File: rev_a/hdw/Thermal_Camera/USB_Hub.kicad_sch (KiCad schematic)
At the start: 1 part

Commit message: duplicated telemetry for all rails, added random tweaks to logic levels of signals
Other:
- note added: "CONSIDER CHANGING TO TUSB2046"
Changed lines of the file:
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@@
     (company "Drew Maatman and Michael Laffin")
+  )
+  (text "CONSIDER CHANGING TO TUSB2046" (at 72.39 38.735 0)
+    (effects (font (face "Courier New") (size 5.08 5.08) (thickness 1.016) bold (color 194 0 0 1)) (justify left bottom))
   )
   (symbol (lib_id "Interface_USB:TUSB2036") (at 131.445 91.44 0) (mirror y) (unit 1)

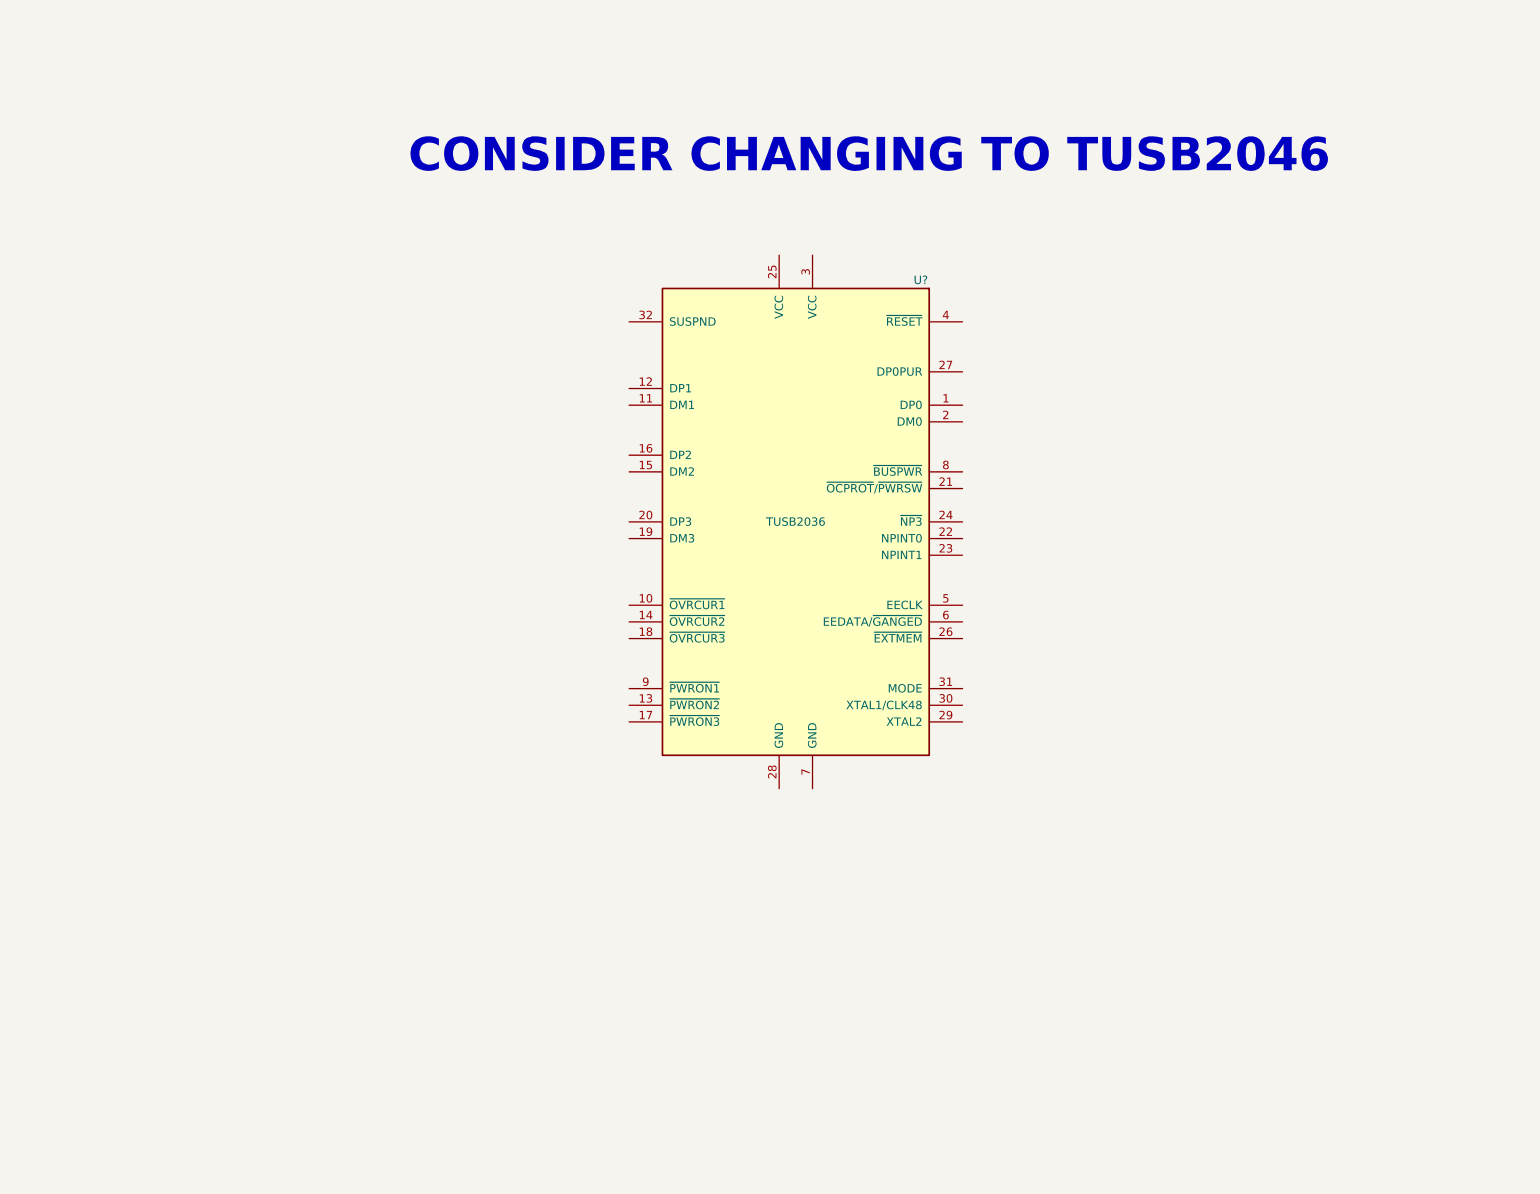
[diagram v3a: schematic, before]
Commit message: added some USB stuff
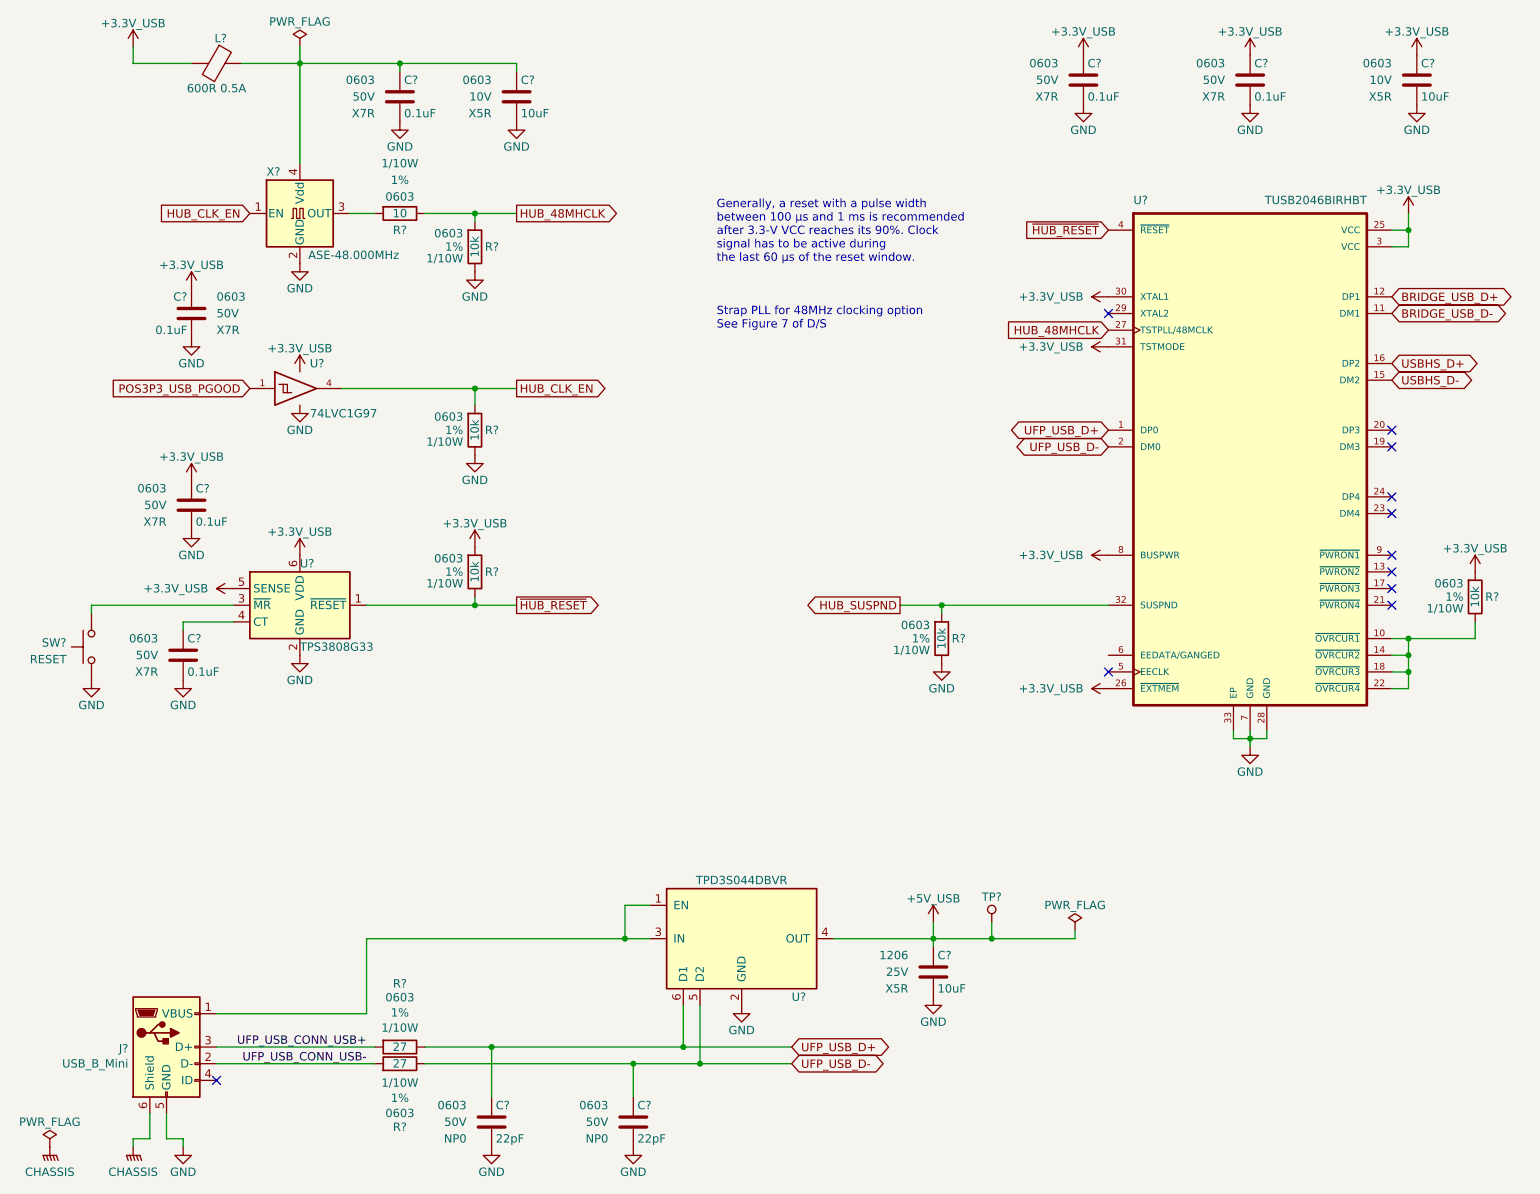
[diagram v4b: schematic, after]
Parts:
- removed U?: TUSB2036, Package_QFP:LQFP-32_7x7mm_P0.8mm, symbol Interface_USB:TUSB2036
- added C? (x6): 0.1uF, Capacitors_SMD:C_0603, symbol Custom_Library:C_Custom
- added C?: 10uF, Capacitors_SMD:C_1206, symbol Custom_Library:C_Custom
- added C? (x2): 10uF, Capacitors_SMD:C_0603, symbol Custom_Library:C_Custom
- added C? (x2): 22pF, Capacitors_SMD:C_0603, symbol Custom_Library:C_Custom
- added J?: USB_B_Mini, Connectors:USB_Mini-B, symbol Connector:USB_B_Mini
- added L?: 600R 0.5A, Inductors_SMD:L_0603, symbol Device:Ferrite_Bead
- added R? (x5): 10k, Resistors_SMD:R_0603, symbol Custom_Library:R_Custom
- added R? (x2): 27, Resistors_SMD:R_0603, symbol Custom_Library:R_Custom
- added R?: 10, Resistors_SMD:R_0603, symbol Custom_Library:R_Custom
- added SW?: RESET, Button_Switch_THT:SW_PUSH_6mm, symbol Switch:SW_Push
- added TP?: TP, Custom Footprints Library:Test_Point, symbol Custom_Library:TP
- added U?: TPD3S044DBVR, TO_SOT_Packages_SMD:SOT-23-6, symbol Custom_Library:TPD3S014DBVR
- added U?: TUSB2046BIRHBT, Package_DFN_QFN:VQFN-32-1EP_5x5mm_P0.5mm_EP3.5x3.5mm, symbol Custom Library:TUSB2046BIRHBT
- added U?: TPS3808G33, Package_TO_SOT_SMD:SOT-23-6, symbol Power_Supervisor:TPS3808DBV
- added U?: 74LVC1G97, Package_TO_SOT_SMD:SOT-363_SC-70-6, symbol Custom_Library:74LVC1G97_Power_BUF
- added X?: ASE-48.000MHz, Oscillator:Oscillator_SMD_Abracon_ASE-4Pin_3.2x2.5mm, symbol Oscillator:ASE-xxxMHz
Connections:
- new net: C?.1, U?.4 (CT)
- new net: SW?.2, U?.3 (~{MR})
- new net: J?.1 (VBUS), U?.1 (EN), U?.3 (IN)
- new net: C?.1, C?.1, L?.1, X?.4 (Vdd)
- new net: R?.2, U?.10 (~{OVRCUR1}), U?.14 (~{OVRCUR2}), U?.18 (~{OVRCUR3}), U?.22 (~{OVRCUR4})
- new net: R?.1, X?.3 (OUT)
- new net +3.3V_USB: C?.1, C?.1, C?.1, C?.1, C?.1, L?.2, R?.1, R?.1, U?.25 (VCC), U?.26 (~{EXTMEM}), U?.3 (VCC), U?.30 (XTAL1), U?.31 (TSTMODE), U?.5 (SENSE), U?.5 (VCC), U?.6 (VDD), U?.8 (BUSPWR)
- new net +5V_USB: C?.1, TP?.1 (TP), U?.4 (OUT)
- new net BRIDGE_USB_D+: U?.12 (DP1)
- new net BRIDGE_USB_D-: U?.11 (DM1)
- new net CHASSIS: J?.6 (Shield)
- new net GND: C?.2, C?.2, C?.2, C?.2, C?.2, C?.2, C?.2, C?.2, C?.2, C?.2, C?.2, J?.5 (GND), R?.2, R?.2, R?.2, SW?.1, U?.2 (GND), U?.2 (GND), U?.2 (GND), U?.28 (GND), U?.3 (GND), U?.33 (EP), U?.6 (GND), U?.7 (GND), X?.2 (GND)
- new net HUB_48MHCLK: R?.1, R?.2, U?.27 (TSTPLL/48MCLK)
- new net HUB_CLK_EN: R?.1, U?.4, X?.1 (EN)
- new net HUB_SUSPND: R?.1, U?.32 (SUSPND)
- new net POS3P3_USB_PGOOD: U?.1
- new net UFP_USB_CONN_USB+: J?.3 (D+), R?.1
- new net UFP_USB_CONN_USB-: J?.2 (D-), R?.1
- new net UFP_USB_D+: C?.1, R?.2, U?.1 (DP0), U?.6 (D1)
- new net UFP_USB_D-: C?.1, R?.2, U?.2 (DM0), U?.5 (D2)
- new net USBHS_D+: U?.16 (DP2)
- new net USBHS_D-: U?.15 (DM2)
- new net ~{HUB_RESET}: R?.2, U?.1 (~{RESET}), U?.4 (~{RESET})
- no-connect marks 0 -> 11
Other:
- note added: "Generally, a reset with a pulse width between 100 μs and 1 ms is recommended after 3.3-V VCC reaches its 90%. Clock signal has to be active during the last 60 μs of the reset window."
- note added: "Strap PLL for 48MHz clocking option See Figure 7 of D/S"
- note removed: "CONSIDER CHANGING TO TUSB2046"

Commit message: added some more USB stuff
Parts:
- removed C?: 10uF, Capacitors_SMD:C_1206, symbol Custom_Library:C_Custom
- removed C? (x2): 22pF, Capacitors_SMD:C_0603, symbol Custom_Library:C_Custom
- removed J?: USB_B_Mini, Connectors:USB_Mini-B, symbol Connector:USB_B_Mini
- removed R? (x2): 27, Resistors_SMD:R_0603, symbol Custom_Library:R_Custom
- removed TP?: TP, Custom Footprints Library:Test_Point, symbol Custom_Library:TP
- removed U?: TPD3S044DBVR, TO_SOT_Packages_SMD:SOT-23-6, symbol Custom_Library:TPD3S014DBVR
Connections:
- net GND: now also U?.6 (EEDATA/GANGED)
- no-connect marks 11 -> 10

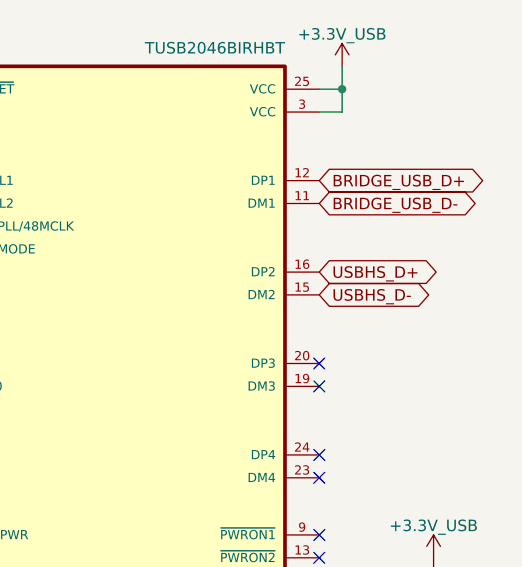
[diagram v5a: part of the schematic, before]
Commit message: added pull resistors for LCD signals
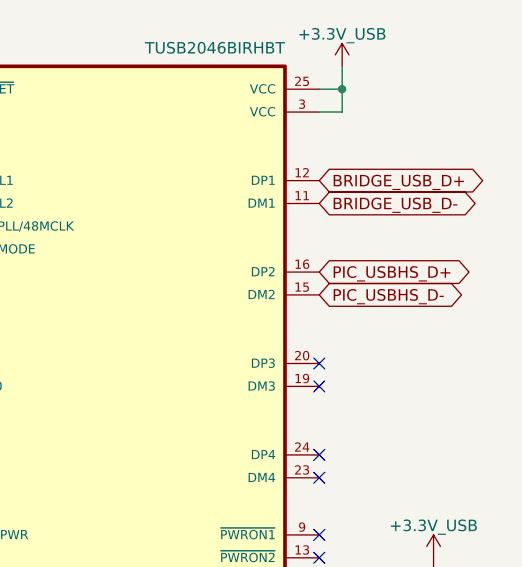
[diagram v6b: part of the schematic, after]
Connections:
- net USBHS_D+ renamed PIC_USBHS_D+
- net USBHS_D- renamed PIC_USBHS_D-
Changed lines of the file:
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@@
     )
   )
-  (global_label "USBHS_D-" (shape bidirectional) (at 222.25 69.85 0) (fields_autoplaced)
+  (global_label "PIC_USBHS_D-" (shape bidirectional) (at 222.25 69.85 0) (fields_autoplaced)
     (effects (font (size 1.27 1.27)) (justify left))
-    (property "Intersheetrefs" "${INTERSHEET_REFS}" (at 236.4271 69.85 0)
+    (property "Intersheetrefs" "${INTERSHEET_REFS}" (at 240.5395 69.85 0)
       (effects (font (size 1.27 1.27)) (justify left) hide)
     )
   )
-  (global_label "USBHS_D+" (shape bidirectional) (at 222.25 67.31 0) (fields_autoplaced)
+  (global_label "PIC_USBHS_D+" (shape bidirectional) (at 222.25 67.31 0) (fields_autoplaced)
     (effects (font (size 1.27 1.27)) (justify left))
-    (property "Intersheetrefs" "${INTERSHEET_REFS}" (at 236.4271 67.31 0)
+    (property "Intersheetrefs" "${INTERSHEET_REFS}" (at 240.5395 67.31 0)
       (effects (font (size 1.27 1.27)) (justify left) hide)
     )

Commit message: lots of random schematic progress
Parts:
- added R?: 10k, Resistors_SMD:R_0603, symbol Custom_Library:R_Custom
- added U?: 74LVC1G97, Package_TO_SOT_SMD:SOT-363_SC-70-6, symbol Custom_Library:74LVC1G97_Power_BUF
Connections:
- net +3.3V_USB: now also U?.5 (VCC)
- net GND: now also R?.2, U?.2 (GND), U?.3 (GND), U?.6 (GND)
- net HUB_SUSPND: now also R?.1, U?.4; no longer R?.1, U?.32 (SUSPND)
- new net: R?.1, U?.1, U?.32 (SUSPND)
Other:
- moved on the sheet: R?
